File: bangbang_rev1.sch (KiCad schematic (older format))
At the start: 0 parts

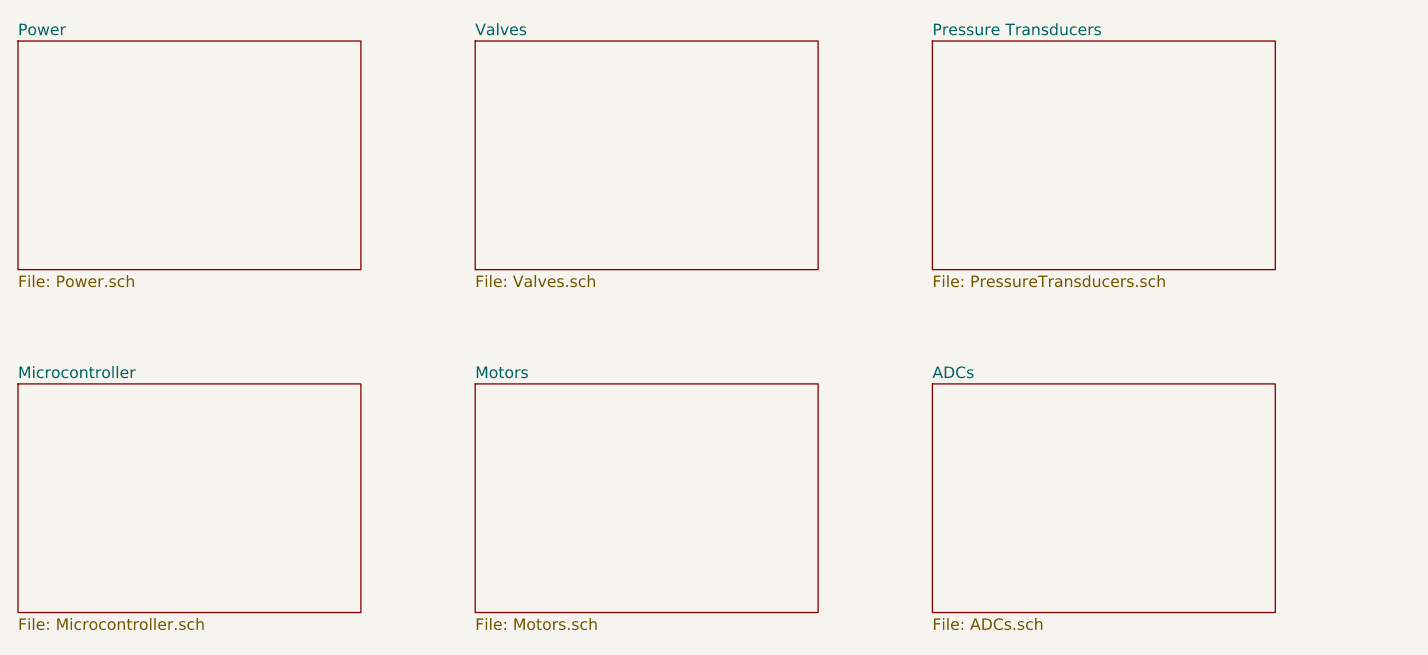
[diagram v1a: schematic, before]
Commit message: finished up uC sheet and pressure transducers
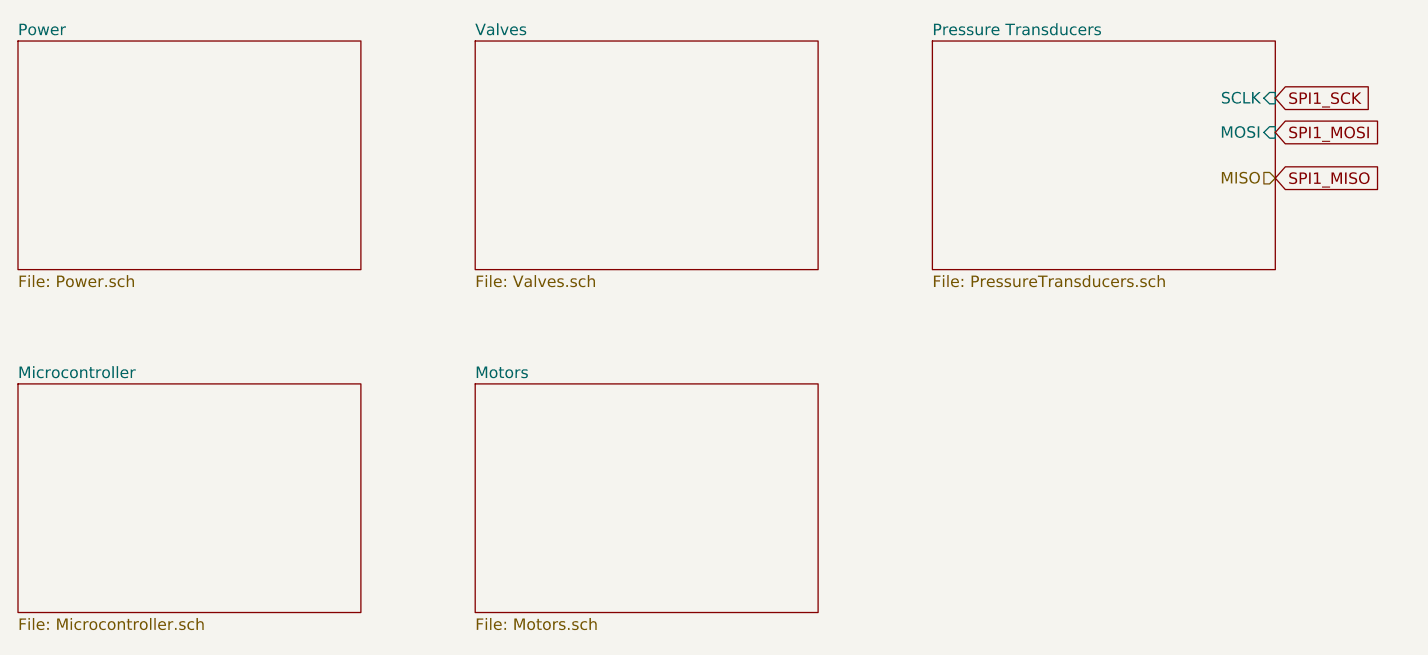
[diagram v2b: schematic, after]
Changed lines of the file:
@@
 $Descr A4 11693 8268
 encoding utf-8
-Sheet 1 10
+Sheet 1 11
 Title ""
 Date ""
@@
 F0 "Pressure Transducers" 50
 F1 "PressureTransducers.sch" 50
+F2 "SCLK" I R 6500 1750 50
+F3 "MOSI" I R 6500 1900 50
 $EndSheet
 $Sheet
@@
 F1 "Motors.sch" 50
 $EndSheet
-$Sheet
-S 5000 3000 1500 1000
-U 5E49EA75
-F0 "ADCs" 50
-F1 "ADCs.sch" 50
-$EndSheet
+Text HLabel 6500 2100 0    50   Input ~ 0
+MISO
+Text GLabel 6500 1750 2    50   Input ~ 0
+SPI1_SCK
+Text GLabel 6500 1900 2    50   Input ~ 0
+SPI1_MOSI
+Text GLabel 6500 2100 2    50   Input ~ 0
+SPI1_MISO
 $EndSCHEMATC

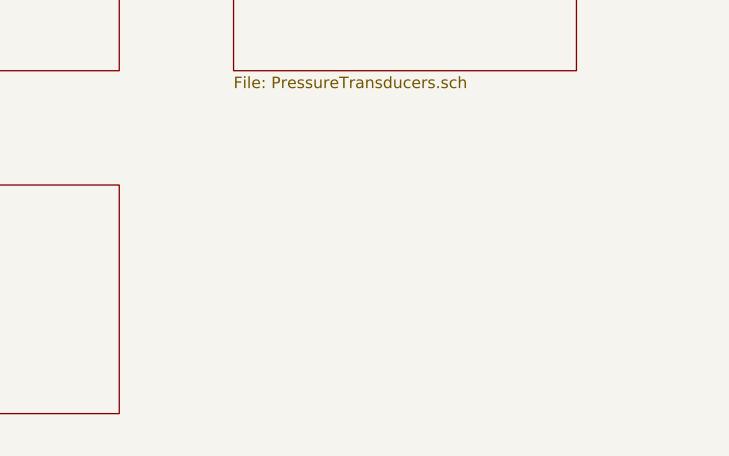
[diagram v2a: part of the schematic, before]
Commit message: Valves and ducers
Finished valves and ducers and their connectors. Got rid of 4 pin ducers. Made all ducers powered by +5V. Cleaned up some uneeded files.
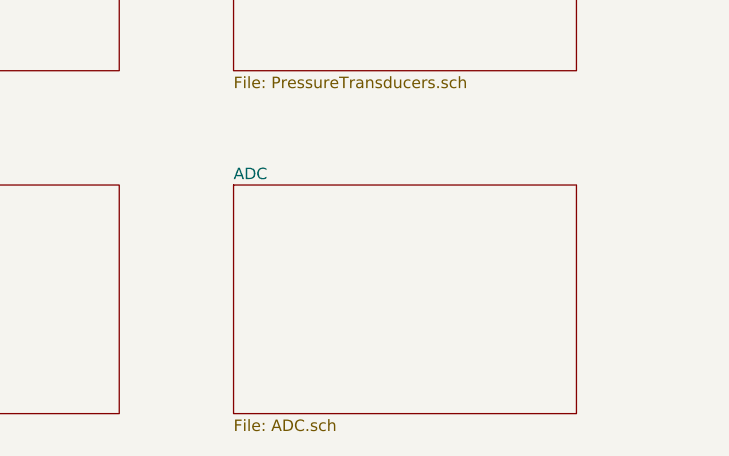
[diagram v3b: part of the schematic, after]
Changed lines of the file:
@@
 Text GLabel 6500 2100 2    50   Input ~ 0
 SPI1_MISO
+$Sheet
+S 5000 3000 1500 1000
+U 5E63996E
+F0 "ADC" 50
+F1 "ADC.sch" 50
+$EndSheet
 $EndSCHEMATC

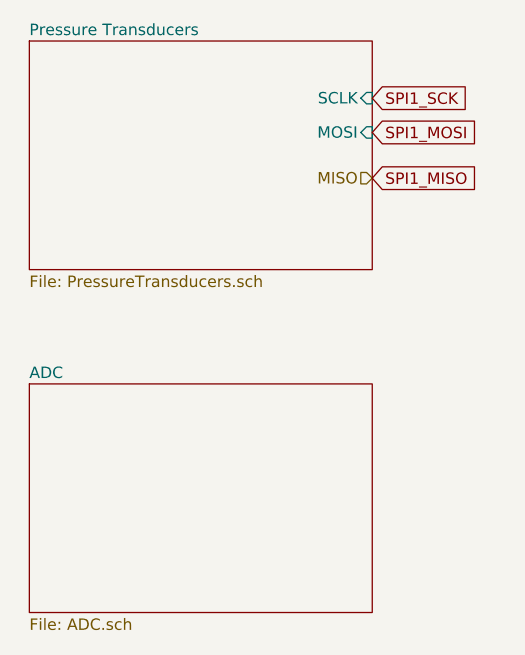
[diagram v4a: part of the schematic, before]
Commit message: hotfix
Spi labels moved to correct location
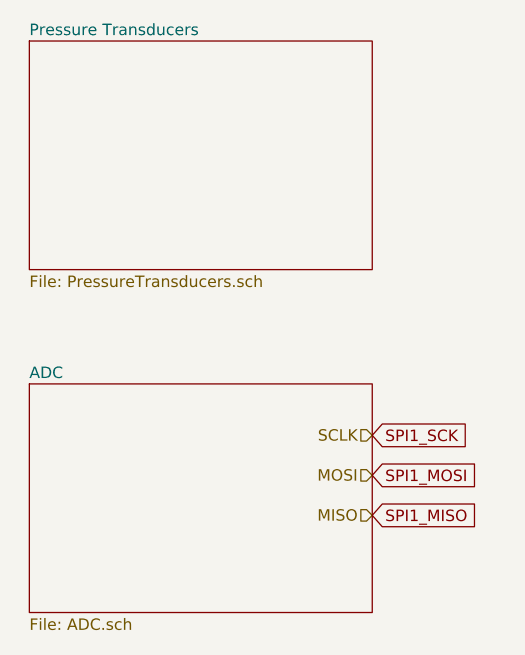
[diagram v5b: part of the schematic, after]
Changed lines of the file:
@@
 F0 "Pressure Transducers" 50
 F1 "PressureTransducers.sch" 50
-F2 "SCLK" I R 6500 1750 50
-F3 "MOSI" I R 6500 1900 50
 $EndSheet
 $Sheet
@@
 F1 "Motors.sch" 50
 $EndSheet
-Text HLabel 6500 2100 0    50   Input ~ 0
-MISO
-Text GLabel 6500 1750 2    50   Input ~ 0
+Text GLabel 6500 3225 2    50   Input ~ 0
 SPI1_SCK
-Text GLabel 6500 1900 2    50   Input ~ 0
+Text GLabel 6500 3400 2    50   Input ~ 0
 SPI1_MOSI
-Text GLabel 6500 2100 2    50   Input ~ 0
+Text GLabel 6500 3575 2    50   Input ~ 0
 SPI1_MISO
 $Sheet
@@
 F1 "ADC.sch" 50
 $EndSheet
+Text HLabel 6500 3225 0    50   Input ~ 0
+SCLK
+Text HLabel 6500 3400 0    50   Input ~ 0
+MOSI
+Text HLabel 6500 3575 0    50   Input ~ 0
+MISO
 $EndSCHEMATC

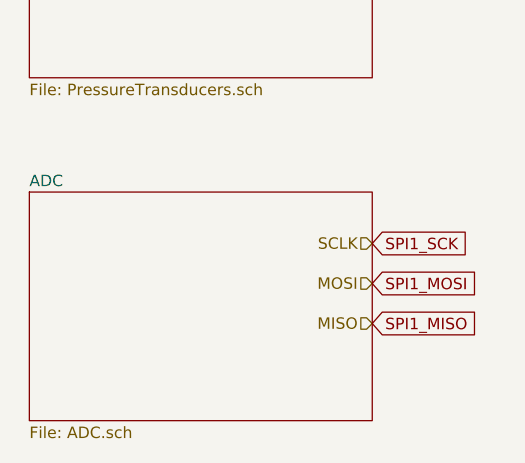
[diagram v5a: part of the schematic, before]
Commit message: hotfix
fixed some labels
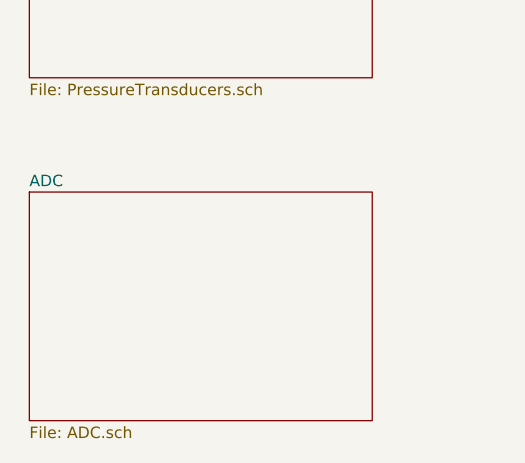
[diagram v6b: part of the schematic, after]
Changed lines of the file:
@@
+$EndSheet
+$Sheet
+S 5000 3000 1500 1000
+U 5E63996E
+F0 "ADC" 50
+F1 "ADC.sch" 50
 $EndSheet
 $Sheet
@@
 F1 "Motors.sch" 50
 $EndSheet
-Text GLabel 6500 3225 2    50   Input ~ 0
-SPI1_SCK
-Text GLabel 6500 3400 2    50   Input ~ 0
-SPI1_MOSI
-Text GLabel 6500 3575 2    50   Input ~ 0
-SPI1_MISO
-$Sheet
-S 5000 3000 1500 1000
-U 5E63996E
-F0 "ADC" 50
-F1 "ADC.sch" 50
-$EndSheet
-Text HLabel 6500 3225 0    50   Input ~ 0
-SCLK
-Text HLabel 6500 3400 0    50   Input ~ 0
-MOSI
-Text HLabel 6500 3575 0    50   Input ~ 0
-MISO
 $EndSCHEMATC
